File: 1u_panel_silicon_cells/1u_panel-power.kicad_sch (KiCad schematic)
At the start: 70 parts, among them J1 MMS-104-01-[F/L]-SH, Q1 DMP3050LVT-7, Q2 DMP2240UDM-7, U10 TPS63060DSCR, U12 LTC4412, U3 LT1618EMSTRPBF, U4 INA226

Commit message: changes for silicon solar module bringup tasks
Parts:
- removed Q1: DMP3050LVT-7, Package_TO_SOT_SMD:SOT-23-6, symbol oresat-transistors:DMP3050LVT-7
- removed R34, R35: 100, oresat-passives:0603-C-NOSILK, symbol Device:R_US
- removed TP5: TEST-POINT-LARGE-SQUARE, oresat-misc:TestPoint-0.75mm-th, symbol oresat-misc:Test-Point-0.75mm-th
- added C37: 100n, oresat-passives:0603-C-NOSILK, symbol Device:C
- added Q1: NTR4101P, Package_TO_SOT_SMD:SOT-23, symbol Transistor_FET:NTR2101P
- R36, R37: value 100 -> 10; DPN RMCF0603FT100RTR-ND -> RMCF0603FT10R0CT-ND; MFR Stackpole Electronics Inc -> Stackpole Electronics Inc; MPN RMCF0603FT100R -> RMCF0603FT10R0
- U3: footprint Package_SO:MSOP-10_3x3mm_P0.5mm -> oresat-ics:MSOP-10_MS
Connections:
- net SCL: now also U4.5 (SCL); no longer U4.4 (SDA)
- net SDA: now also U4.4 (SDA); no longer U4.5 (SCL)
- net VMPPT: now also Q1.2 (S)
- net VSOLAR: now also U3.3 (ISP)
- net ~{SHDN-OUPUT}: now also Q1.1 (G)
- net at L2.1, R17.2: now also R36.1, U3.2 (ISN); no longer R36.2
- net at R37.1, U4.10 (Vin+): now also C37.1; no longer U4.8 (Vbus)
- net at U12.3 (CTL): now also Q1.3 (D)
- net at U4.9 (Vin-): now also R36.2, U4.8 (Vbus), C37.2; no longer R36.1

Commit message: chages for https://github.com/oresat/oresat-solar-hardware/issues/53
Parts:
- removed R17: 0.1, oresat-passives:0805-C-NOSILK, symbol Device:R_US
- removed TP26, TP27, TP28, TP29: TEST-POINT-LARGE-SQUARE, oresat-misc:TestPoint-0.75mm-th, symbol oresat-misc:Test-Point-0.75mm-th
- added R17: 100m, oresat-passives:1206-C, symbol oresat-batteries-eagle-import:R-US_1206-C
- added TP17, TP18, TP5, TP8: TEST-POINT-LARGE-SQUARE, oresat-misc:TestPoint-0.75mm-th, symbol oresat-misc:Test-Point-0.75mm-th
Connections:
- net GND: now also TP17.1, TP18.1, TP5.1, TP8.1
- net VSOLAR: now also R17.1
- net at L2.1, R36.1, U3.2 (ISN): now also R17.2
- net at C37.1, R37.1, U4.10 (Vin+): now also U4.8 (Vbus)
- net at C37.2, R36.2, U4.9 (Vin-): no longer U4.8 (Vbus)
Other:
- note added: "1206"
- note added: "Ground Test Points"
- note added: "Raise to 1uF if too noisy"

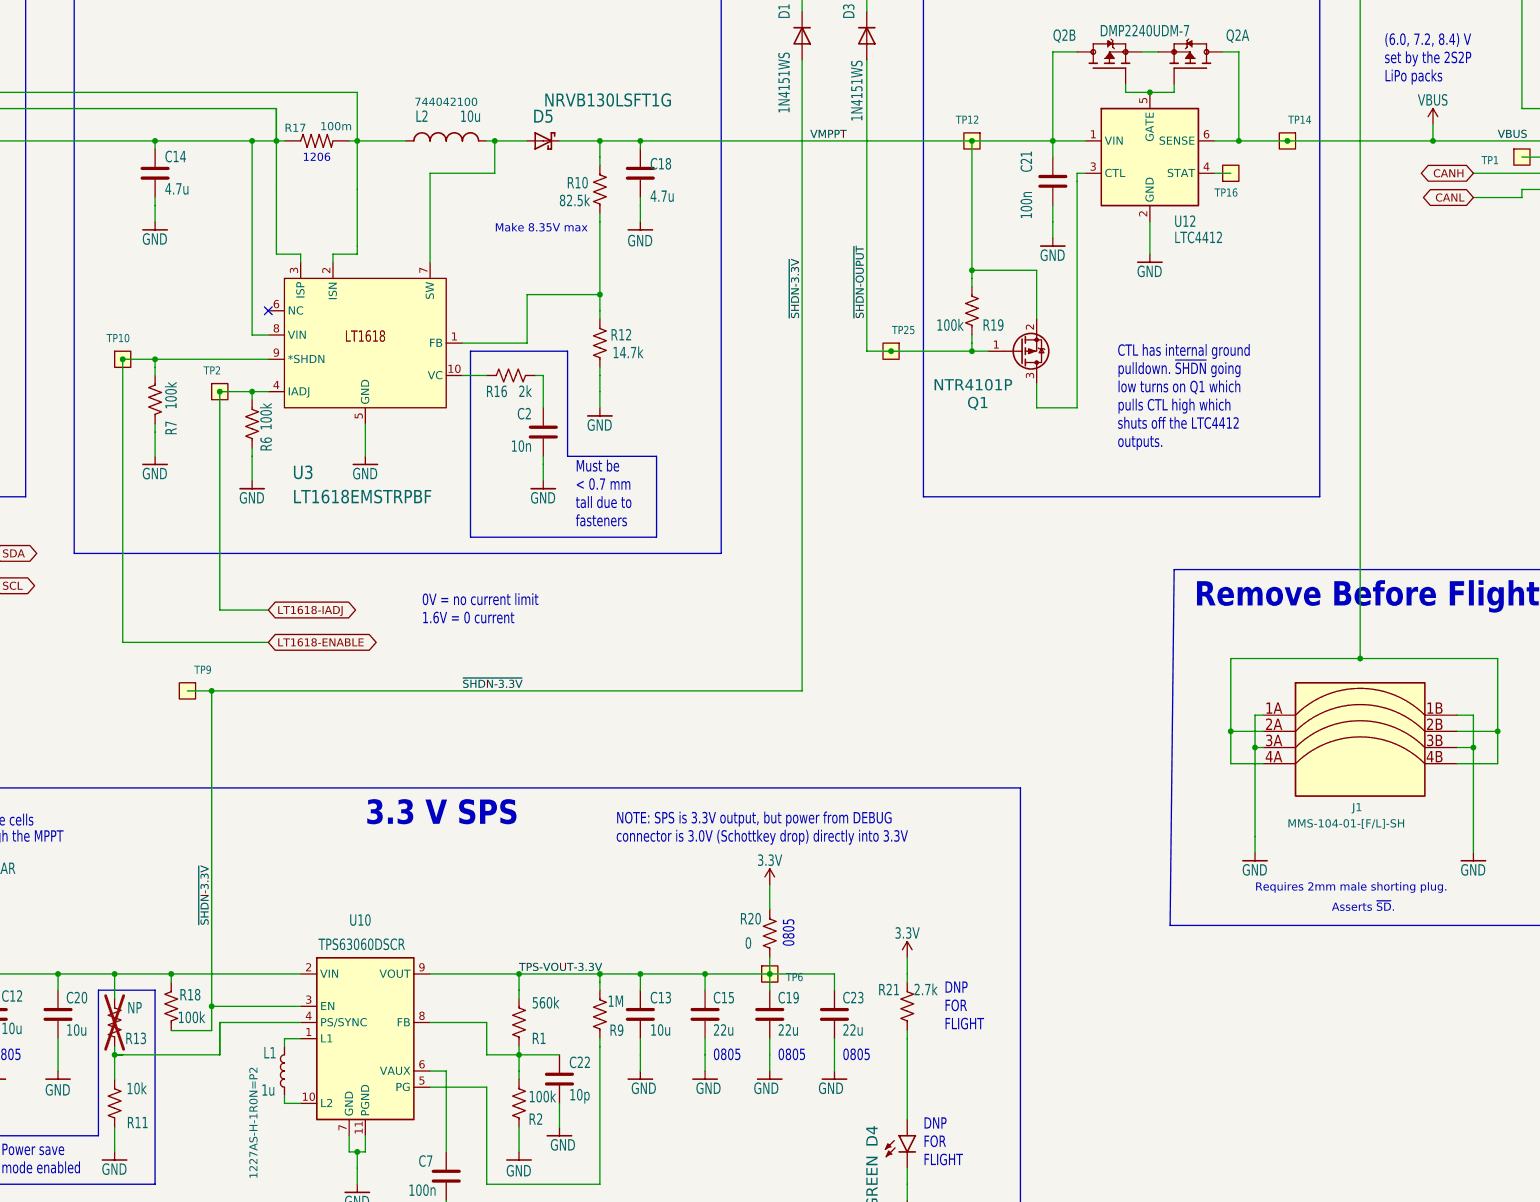
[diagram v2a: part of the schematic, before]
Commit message: changes for bringup issues on Si Solar module
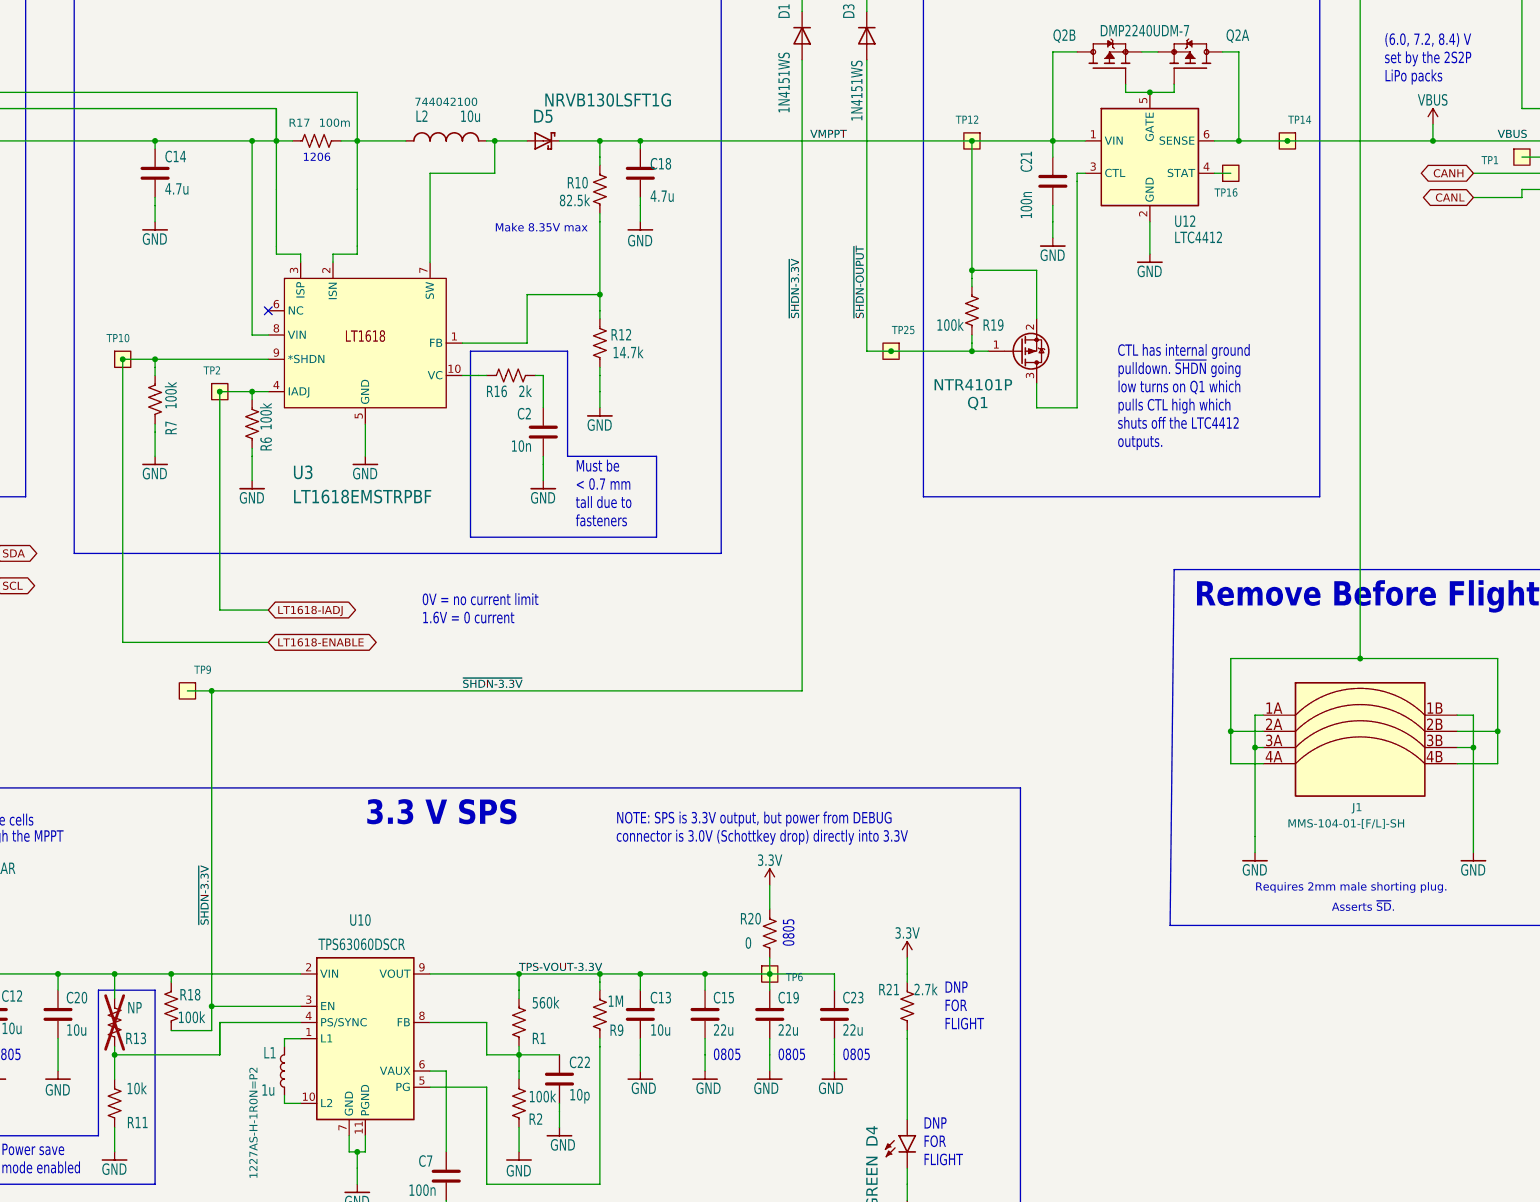
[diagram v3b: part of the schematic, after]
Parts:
- R17: symbol oresat-batteries-eagle-import:R-US_1206-C -> Device:R_US

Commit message: Cleanup before fab! Added pullup resistors to ALERTs on TMP101s, removed some paranoia hardware including test points and pullups we don't need, did some schematic polishing for prettiness, and cleaned up some of the zones onthe layout. Removed the need for any old import or local symbol or footprint libraries. Upgraded to v1.1.
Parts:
- removed PCB1: ORESAT-SOLAR-BOARD-V1.0-SILICON-CELLS, oresat-pcbs:ORESAT-SOLAR-BOARD-V4, symbol 1u_panel-eagle-import:ORESAT-SOLAR-BOARD-V4-SPECTROLABS
- removed R9: 1M, oresat-passives:0603-C-NOSILK, symbol Device:R_US
- removed TP16: TEST-POINT-LARGE-SQUARE, oresat-misc:TestPoint-0.75mm-th, symbol oresat-misc:Test-Point-0.75mm-th
- removed U$1: FLIGHMARKERNEW, oresat-graphics:FLIGHTMARKER_NEW_BOARDS, symbol 1u_panel-eagle-import:FLIGHMARKERNEW
- removed U$2, U$3, U$4: FIDUCIAL, Fiducial:Fiducial_1mm_Mask2mm, symbol 1u_panel-eagle-import:FIDUCIAL
- C12, C13, C14, C15, C18, C19, C2, C20, C21, C22, C23, C37, C4, C6, C7, C8, CF1, D1, D3, J1, L1, L2, Q2, R1, R10, R11, R12, R14, R16, R18, R19, R2, R20, R21, R36, R37, R6, R7, U10, U12, U3, U4: Distributor Digi-Key -> (none)
- D4: value GREEN -> GRN; footprint oresat-diodes:LED-0603 -> LED_SMD:LED_0603_1608Metric; symbol 1u_panel-eagle-import:LED-GREEN0603 -> Device:LED_Small_Filled; Distributor Digi-Key -> (none)
- D5: footprint oresat-diodes:SOD123 -> Diode_SMD:D_SOD-123; symbol 1u_panel-eagle-import:NRVB130TGSOD123 -> Device:D_Schottky; Distributor Digi-Key -> (none)
- Q1: DST Digi-Key -> (none)
- R13: value NP -> 10k; Distributor Digi-Key -> (none); now fitted; now in the parts list
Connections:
- net 3.3V: now also R13.2
- net GND: now also D4.1 (K); no longer D4.C
- net VMPPT: now also D5.1 (K); no longer D5.K (CATHODE)
- net at R21.2: now also D4.2 (A); no longer D4.A
- net at C12.1, C20.1, R14.1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: no longer R13.2
- net at R11.2, U10.4 (PS/SYNC): no longer R13.1
- net at L2.2, U3.7 (SW): now also D5.2 (A); no longer D5.A (ANODE)
- net INA226-nALERT: now reaches TP24.1, U4.3 (~{Alert})
- net INA226-nALERT: now also R13.1
- no-connect marks 1 -> 3
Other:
- note added: "EXTREMELY IMPORTANT ALL COMPONENTS ON TOP LAYER MUST BE < 2 MM TALL ALL COMPONENTS ON TOP LAYER WITH FASTENERS BELOW THEM MUST BE < 0.7 MM TALL CHECK USER.DRAWINGS LAYER FOR FASTNER PLACEMENT"
- note removed: "ALL COMPONENTS ABOVE FASTENERS MUST BE < 0.7 MM TALL"
- note removed: "ALL COMPONENTS MUST BE < 2.0 MM TALL"
- note removed: "Fiducials"
- note removed: "Must be < 0.7 mm tall due to fasteners"
- moved on the sheet: C12, C13, C14, C15, C18, C19, C2, C20, C21, C22, C23, C37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
